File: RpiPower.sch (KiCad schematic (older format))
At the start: 17 parts, among them P1 header_pin, P2 Rpi_HDR-40, P3 header_pin, P4 header_pin, P5 header_pin, Q1 2N7002, Q2 2N7002, SW1 SW_PUSH, SW2 SW_PUSH

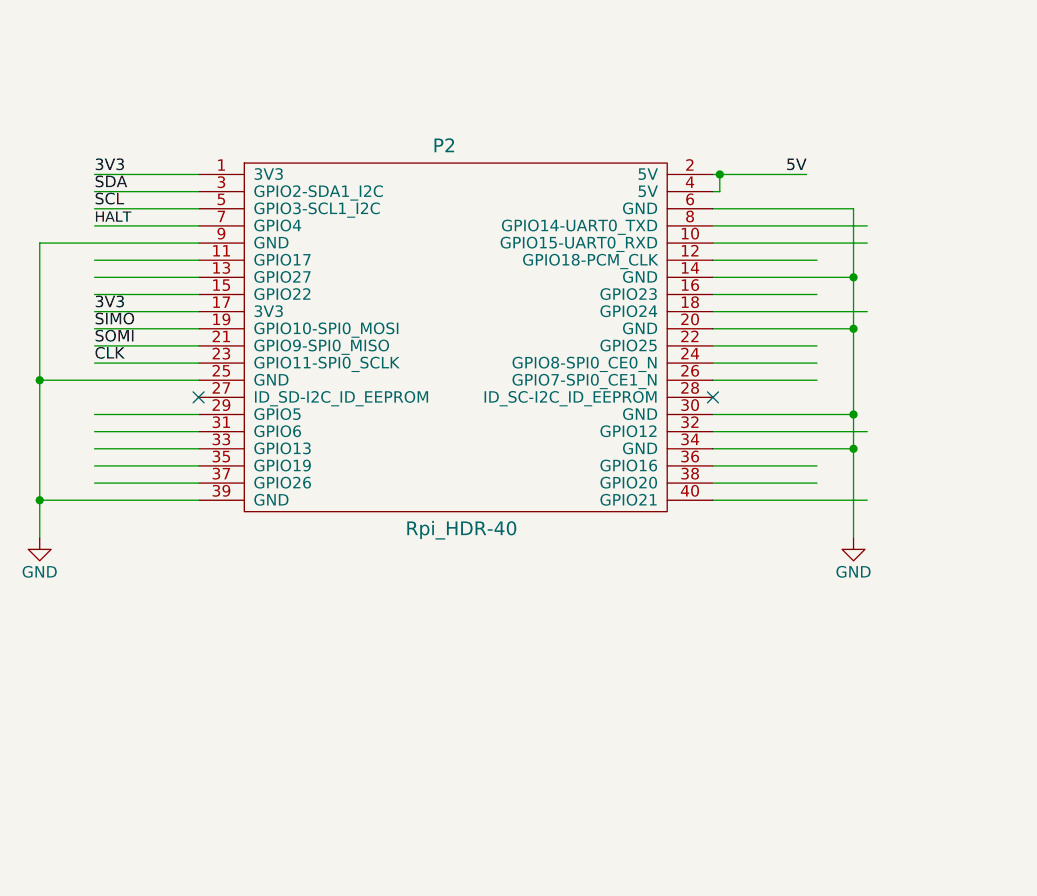
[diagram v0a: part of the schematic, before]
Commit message: changed from Raspberry pi 40-pin header to single pin headers to make the pcb smaller (cut size in half so half the cost)
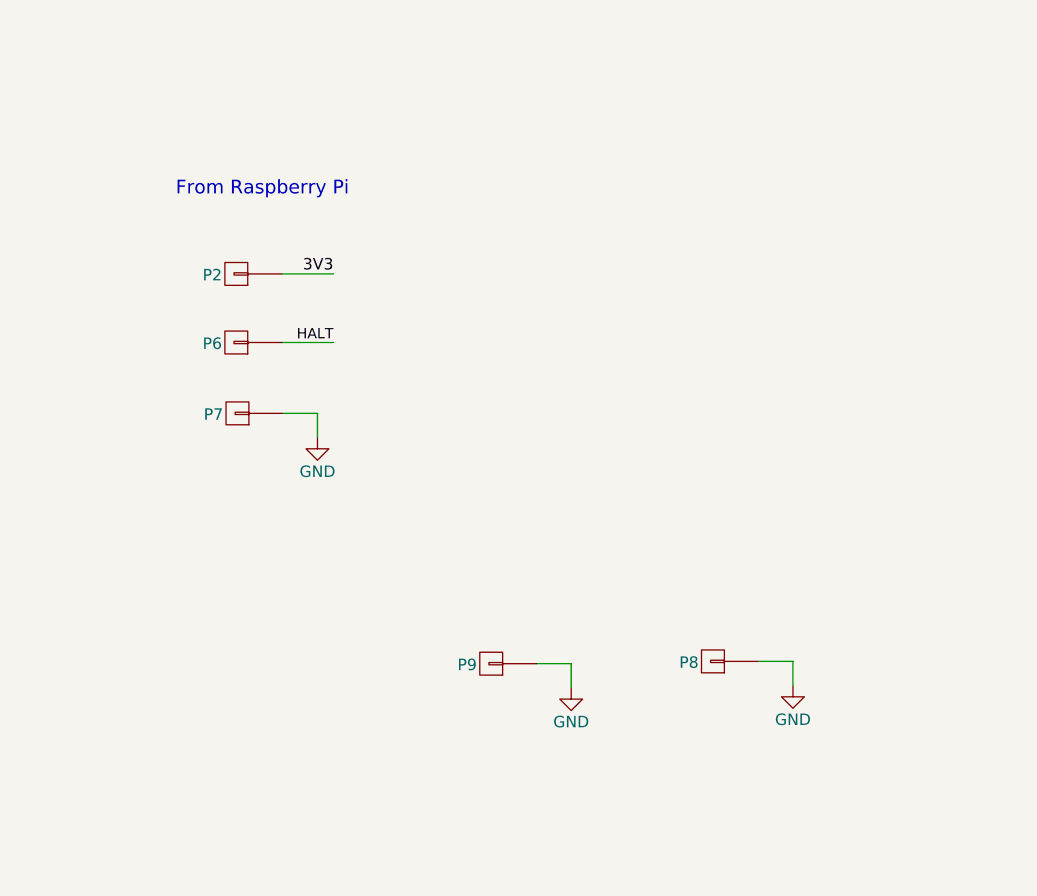
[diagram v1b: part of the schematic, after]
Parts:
- removed P2: Rpi_HDR-40, footprints_on_Cdrive:header_2x20, symbol Rpi_HDR-40
- added P2, P6, P7, P8, P9: header_pin, footprints_on_Cdrive:Hdr_Pin, symbol header_pin
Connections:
- net labels removed: 5V, CLK, SCL, SDA, SIMO, SOMI
- wire segments 65 -> 32
- no-connect marks 2 -> 0
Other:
- note added: "From Raspberry Pi"
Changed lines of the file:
@@
 $EndDescr
-$Comp
-L Rpi_HDR-40 P2
-U 1 1 59291121
-P 2630 2995
-F 0 "P2" H 3780 3120 60  0000 C CNN
-F 1 "Rpi_HDR-40" H 3855 1445 60  0000 C CNN
-F 2 "footprints_on_Cdrive:header_2x20" H 3845 1425 60  0001 C CNN
-F 3 "" H 3845 1425 60  0000 C CNN
-F 4 "dual_row_header_pins" H 2630 2995 60  0001 C CNN "supplier pn"
-	1    2630 2995
-	1    0    0    -1
-$EndComp
-Text Label 2250 3745 0    50   ~ 0
-SOMI
-Text Label 5365 2995 2    50   ~ 0
-5V
-Text Label 2250 3670 0    50   ~ 0
-SIMO
-$Comp
-L GND #PWR01
-U 1 1 59291186
-P 5570 4585
-F 0 "#PWR01" H 5570 4335 50  0001 C CNN
-F 1 "GND" H 5570 4435 50  0000 C CNN
-F 2 "" H 5570 4585 60  0000 C CNN
-F 3 "" H 5570 4585 60  0000 C CNN
-	1    5570 4585
-	1    0    0    -1
-$EndComp
-$Comp
-L GND #PWR02
-U 1 1 5929118C
-P 2010 4585
-F 0 "#PWR02" H 2010 4335 50  0001 C CNN
-F 1 "GND" H 2010 4435 50  0000 C CNN
-F 2 "" H 2010 4585 60  0000 C CNN
-F 3 "" H 2010 4585 60  0000 C CNN
-	1    2010 4585
-	1    0    0    -1
-$EndComp
-Wire Wire Line
-	2705 3745 2250 3745
-Wire Wire Line
-	2705 4345 2250 4345
-Wire Wire Line
-	5410 3820 4955 3820
-Wire Wire Line
-	2705 2995 2250 2995
-Wire Wire Line
-	2705 3070 2250 3070
-Wire Wire Line
-	2705 3145 2250 3145
-Wire Wire Line
-	2705 3670 2250 3670
-Wire Wire Line
-	2705 3220 2250 3220
-Wire Wire Line
-	2705 3370 2250 3370
-Wire Wire Line
-	4955 3220 5630 3220
-Wire Wire Line
-	4955 3295 5630 3295
-Wire Wire Line
-	2705 3445 2250 3445
-Wire Wire Line
-	5410 3370 4955 3370
-Wire Wire Line
-	5410 3520 4955 3520
-Wire Wire Line
-	4955 3145 5570 3145
-Wire Wire Line
-	5570 3145 5570 4585
-Wire Wire Line
-	4955 4195 5570 4195
-Connection ~ 5570 4195
-Wire Wire Line
-	4955 4045 5570 4045
-Connection ~ 5570 4045
-Wire Wire Line
-	4955 3670 5570 3670
-Connection ~ 5570 3670
-Wire Wire Line
-	4955 3445 5570 3445
-Connection ~ 5570 3445
-Wire Wire Line
-	4955 3070 4985 3070
-Wire Wire Line
-	4985 3070 4985 2995
-Connection ~ 4985 2995
-Wire Wire Line
-	2705 3295 2010 3295
-Wire Wire Line
-	2010 3295 2010 4585
-Wire Wire Line
-	2705 3895 2010 3895
-Connection ~ 2010 3895
-Wire Wire Line
-	2705 4420 2010 4420
-Connection ~ 2010 4420
-Wire Wire Line
-	2705 3595 2250 3595
-Wire Wire Line
-	2705 4270 2250 4270
-Wire Wire Line
-	5410 3895 4955 3895
-Wire Wire Line
-	5410 3745 4955 3745
-Wire Wire Line
-	4955 3595 5630 3595
-Wire Wire Line
-	4955 4120 5630 4120
-Wire Wire Line
-	5410 4345 4955 4345
-Wire Wire Line
-	4955 4420 5630 4420
-Text Label 2250 3820 0    50   ~ 0
-CLK
-Wire Wire Line
-	2705 3820 2250 3820
-Wire Wire Line
-	2705 4120 2250 4120
-Wire Wire Line
-	2705 4045 2250 4045
-NoConn ~ 2705 3970
-NoConn ~ 4955 3970
-Wire Wire Line
-	2705 3520 2250 3520
-Text Label 2250 2995 0    50   ~ 0
-3V3
-Wire Wire Line
-	4955 2995 5365 2995
 $Comp
 L 2N7002 Q1
@@
 	7860 2770 7860 2985
 $Comp
-L GND #PWR03
+L GND #PWR01
 U 1 1 592F2DD9
 P 7860 3520
-F 0 "#PWR03" H 7860 3270 50  0001 C CNN
+F 0 "#PWR01" H 7860 3270 50  0001 C CNN
 F 1 "GND" H 7860 3370 50  0000 C CNN
 F 2 "" H 7860 3520 60  0000 C CNN
@@
 	1    0    0    -1
 $EndComp
-Text Label 2250 3595 0    50   ~ 0
-3V3
-Wire Wire Line
-	2705 4195 2250 4195
 $Comp
 L mount_hole MH3
@@
 	1    0    0    -1
 $EndComp
-Wire Wire Line
-	4955 4270 5410 4270
-Text Label 2250 3070 0    50   ~ 0
-SDA
-Text Label 2250 3145 0    50   ~ 0
-SCL
 $Comp
 L SW_PUSH SW1
@@
 $EndComp
 $Comp
-L GND #PWR04
+L GND #PWR02
 U 1 1 59665D02
 P 8380 3695
-F 0 "#PWR04" H 8380 3445 50  0001 C CNN
+F 0 "#PWR02" H 8380 3445 50  0001 C CNN
 F 1 "GND" H 8380 3545 50  0000 C CNN
 F 2 "" H 8380 3695 60  0000 C CNN
@@
 	7850 4560 7850 4775
 $Comp
-L GND #PWR05
+L GND #PWR03
 U 1 1 596674DA
 P 7850 5310
-F 0 "#PWR05" H 7850 5060 50  0001 C CNN
+F 0 "#PWR03" H 7850 5060 50  0001 C CNN
 F 1 "GND" H 7850 5160 50  0000 C CNN
 F 2 "" H 7850 5310 60  0000 C CNN
@@
 $EndComp
 $Comp
-L GND #PWR06
+L GND #PWR04
 U 1 1 596674F9
 P 8370 5485
-F 0 "#PWR06" H 8370 5235 50  0001 C CNN
+F 0 "#PWR04" H 8370 5235 50  0001 C CNN
 F 1 "GND" H 8370 5335 50  0000 C CNN
 F 2 "" H 8370 5485 60  0000 C CNN
@@
 3V3
 $Comp
-L GND #PWR07
+L GND #PWR05
 U 1 1 5966F183
 P 6620 3350
-F 0 "#PWR07" H 6620 3100 50  0001 C CNN
+F 0 "#PWR05" H 6620 3100 50  0001 C CNN
 F 1 "GND" H 6620 3200 50  0000 C CNN
 F 2 "" H 6620 3350 60  0000 C CNN
@@
 	6620 3205 6710 3205
 $Comp
-L GND #PWR08
+L GND #PWR06
 U 1 1 59670428
 P 6635 5135
-F 0 "#PWR08" H 6635 4885 50  0001 C CNN
+F 0 "#PWR06" H 6635 4885 50  0001 C CNN
 F 1 "GND" H 6635 4985 50  0000 C CNN
 F 2 "" H 6635 5135 60  0000 C CNN
@@
 Wire Wire Line
 	8900 3235 8900 3190
-Text Label 2250 3220 0    45   ~ 0
+$Comp
+L header_pin P2
+U 1 1 5980F29E
+P 2870 3430
+F 0 "P2" H 2975 3435 50  0000 C CNN
+F 1 "header_pin" H 2910 3545 50  0001 C CNN
+F 2 "footprints_on_Cdrive:Hdr_Pin" H 2870 3430 60  0001 C CNN
+F 3 "" H 2870 3430 60  0000 C CNN
+	1    2870 3430
+	-1   0    0    1
+$EndComp
+Wire Wire Line
+	3070 3430 3295 3430
+Text Label 3295 3430 2    50   ~ 0
+3V3
+$Comp
+L header_pin P6
+U 1 1 5981079E
+P 2870 3730
+F 0 "P6" H 2975 3735 50  0000 C CNN
+F 1 "header_pin" H 2910 3845 50  0001 C CNN
+F 2 "footprints_on_Cdrive:Hdr_Pin" H 2870 3730 60  0001 C CNN
+F 3 "" H 2870 3730 60  0000 C CNN
+	1    2870 3730
+	-1   0    0    1
+$EndComp
+Wire Wire Line
+	3070 3730 3295 3730
+$Comp
+L header_pin P7
+U 1 1 59810A6F
+P 2875 4040
+F 0 "P7" H 2980 4045 50  0000 C CNN
+F 1 "header_pin" H 2915 4155 50  0001 C CNN
+F 2 "footprints_on_Cdrive:Hdr_Pin" H 2875 4040 60  0001 C CNN
+F 3 "" H 2875 4040 60  0000 C CNN
+	1    2875 4040
+	-1   0    0    1
+$EndComp
+$Comp
+L GND #PWR07
+U 1 1 59810B94
+P 3225 4145
+F 0 "#PWR07" H 3225 3895 50  0001 C CNN
+F 1 "GND" H 3225 3995 50  0000 C CNN
+F 2 "" H 3225 4145 60  0000 C CNN
+F 3 "" H 3225 4145 60  0000 C CNN
+	1    3225 4145
+	-1   0    0    -1
+$EndComp
+Wire Wire Line
+	3075 4040 3225 4040
+Wire Wire Line
+	3225 4040 3225 4145
+Text Label 3295 3730 2    45   ~ 0
 HALT
+Text Notes 2605 3095 0    60   ~ 0
+From Raspberry Pi
+$Comp
+L header_pin P9
+U 1 1 59813A02
+P 3985 5135
+F 0 "P9" H 4090 5140 50  0000 C CNN
+F 1 "header_pin" H 4025 5250 50  0001 C CNN
+F 2 "footprints_on_Cdrive:Hdr_Pin" H 3985 5135 60  0001 C CNN
+F 3 "" H 3985 5135 60  0000 C CNN
+	1    3985 5135
+	-1   0    0    1
+$EndComp
+$Comp
+L GND #PWR08
+U 1 1 59813A08
+P 4335 5240
+F 0 "#PWR08" H 4335 4990 50  0001 C CNN
+F 1 "GND" H 4335 5090 50  0000 C CNN
+F 2 "" H 4335 5240 60  0000 C CNN
+F 3 "" H 4335 5240 60  0000 C CNN
+	1    4335 5240
+	-1   0    0    -1
+$EndComp
+Wire Wire Line
+	4185 5135 4335 5135
+Wire Wire Line
+	4335 5135 4335 5240
+$Comp
+L header_pin P8
+U 1 1 59813AB3
+P 4955 5125
+F 0 "P8" H 5060 5130 50  0000 C CNN
+F 1 "header_pin" H 4995 5240 50  0001 C CNN
+F 2 "footprints_on_Cdrive:Hdr_Pin" H 4955 5125 60  0001 C CNN
+F 3 "" H 4955 5125 60  0000 C CNN
+	1    4955 5125
+	-1   0    0    1
+$EndComp
+$Comp
+L GND #PWR09
+U 1 1 59813AB9
+P 5305 5230
+F 0 "#PWR09" H 5305 4980 50  0001 C CNN
+F 1 "GND" H 5305 5080 50  0000 C CNN
+F 2 "" H 5305 5230 60  0000 C CNN
+F 3 "" H 5305 5230 60  0000 C CNN
+	1    5305 5230
+	-1   0    0    -1
+$EndComp
+Wire Wire Line
+	5155 5125 5305 5125
+Wire Wire Line
+	5305 5125 5305 5230
 $EndSCHEMATC
